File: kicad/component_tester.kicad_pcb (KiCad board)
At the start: 4 copper layers, 100.4 x 83 mm, 81 parts, among them IC201 MCP1640, IC202 ATmega328P-MMH, IC301 FT232RL, IC302 MAX1811, J301 0R-JUMPA, J302 0R-JUMPA, Q201 8 MHz, Q401 BSS138, Q402 BSS138, SW201 EVQ, T201 PMV65XP, T202 BSS84, T203 BSS123, T204 BC847, T301 BSS123, X201 MICRO-USB, X202 ISP

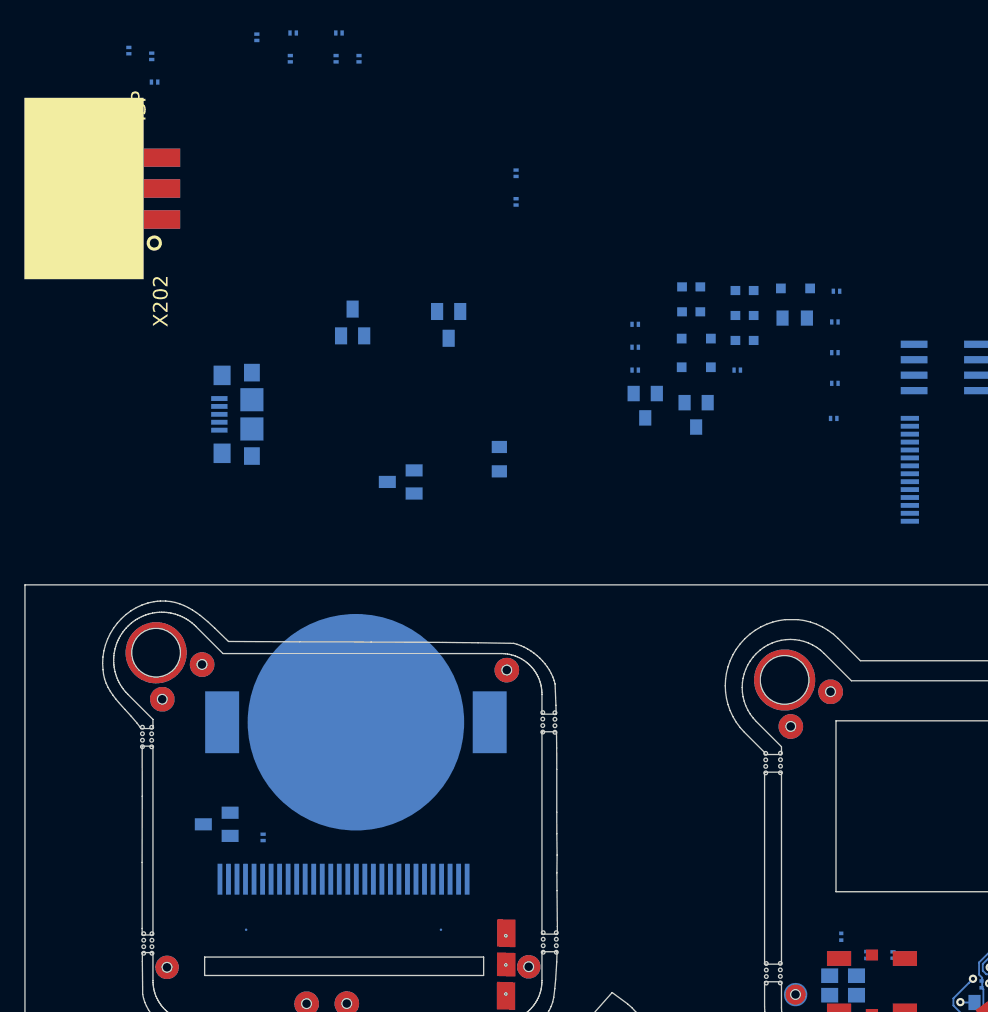
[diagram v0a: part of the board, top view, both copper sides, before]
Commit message: Make ISP header a pogo pin one
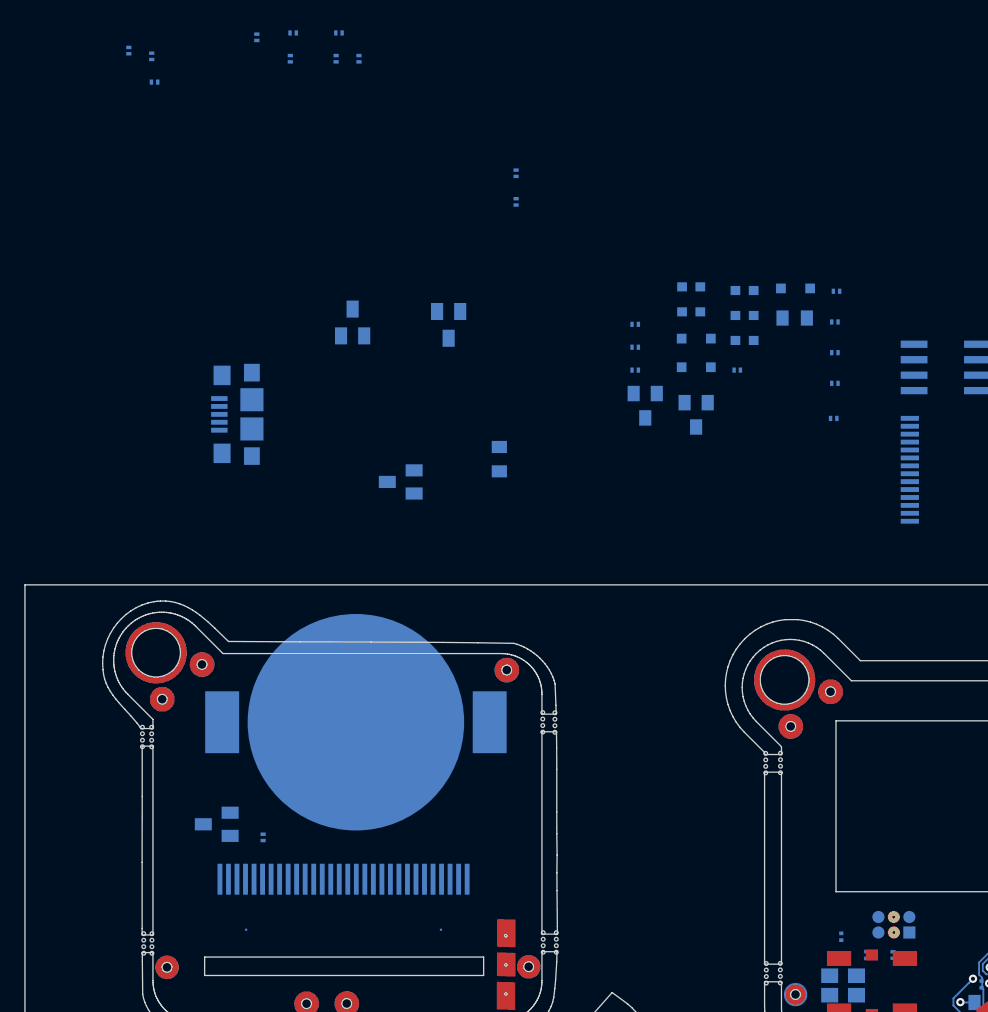
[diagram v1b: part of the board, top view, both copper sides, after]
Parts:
- X202: footprint component_tester:WANNE6_PCBKANTE -> component_tester:Pin_Header_Straight_2x03_Pitch1.27mm; moved to B.Cu
- moved X202 87.7 mm to (162.3, 105.2), turned to 90 degrees
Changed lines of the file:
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@@
     (mod_text_size 1 1)
     (mod_text_width 0.15)
-    (pad_size 0.8 0.8)
-    (pad_drill 0)
+    (pad_size 1 1)
+    (pad_drill 0.2)
     (pad_to_mask_clearance 0.2)
     (aux_axis_origin 0 0)
@@
       (outputformat 1)
       (mirror false)
-      (drillshape 1)
+      (drillshape 0)
       (scaleselection 1)
-      (outputdirectory ""))
+      (outputdirectory ../gerbers/))
   )
   (net 0 "")
@@
     (add_net VCC)
   )
+  (module component_tester:Pin_Header_Straight_2x03_Pitch1.27mm (layer Bottom)
+    (at 162.29 105.15 90)
+    (descr "Through hole straight pin header, 2x03, 1.27mm pitch, double rows")
+    (tags "Through hole pin header THT 2x03 1.27mm double row")
+    (fp_text reference X202 (at 0.635 1.695 90) (layer B.SilkS)
+      (effects (font (size 1 1) (thickness 0.15)) (justify mirror))
+    )
+    (fp_text value ISP (at 0.635 -4.235 90) (layer B.Fab)
+      (effects (font (size 1 1) (thickness 0.15)) (justify mirror))
+    )
+    (fp_line (start -0.2175 0.635) (end 2.34 0.635) (layer B.Fab) (width 0.1))
+    (fp_line (start 2.34 0.635) (end 2.34 -3.175) (layer B.Fab) (width 0.1))
+    (fp_line (start 2.34 -3.175) (end -1.07 -3.175) (layer B.Fab) (width 0.1))
+    (fp_line (start -1.07 -3.175) (end -1.07 -0.2175) (layer B.Fab) (width 0.1))
+    (fp_line (start -1.07 -0.2175) (end -0.2175 0.635) (layer B.Fab) (width 0.1))
+    (fp_line (start -1.13 -3.235) (end -0.30753 -3.235) (layer B.SilkS) (width 0.12))
+    (fp_line (start 1.57753 -3.235) (end 2.4 -3.235) (layer B.SilkS) (width 0.12))
+    (fp_line (start 0.30753 -3.235) (end 0.96247 -3.235) (layer B.SilkS) (width 0.12))
+    (fp_line (start -1.13 -0.76) (end -1.13 -3.235) (layer B.SilkS) (width 0.12))
+    (fp_line (start 2.4 0.695) (end 2.4 -3.235) (layer B.SilkS) (width 0.12))
+    (fp_line (start -1.13 -0.76) (end -0.563471 -0.76) (layer B.SilkS) (width 0.12))
+    (fp_line (start 0.563471 -0.76) (end 0.706529 -0.76) (layer B.SilkS) (width 0.12))
+    (fp_line (start 0.76 -0.706529) (end 0.76 -0.563471) (layer B.SilkS) (width 0.12))
+    (fp_line (start 0.76 0.563471) (end 0.76 0.695) (layer B.SilkS) (width 0.12))
+    (fp_line (start 0.76 0.695) (end 0.96247 0.695) (layer B.SilkS) (width 0.12))
+    (fp_line (start 1.57753 0.695) (end 2.4 0.695) (layer B.SilkS) (width 0.12))
+    (fp_line (start -1.13 0) (end -1.13 0.76) (layer B.SilkS) (width 0.12))
+    (fp_line (start -1.13 0.76) (end 0 0.76) (layer B.SilkS) (width 0.12))
+    (fp_line (start -1.6 1.15) (end -1.6 -3.7) (layer B.CrtYd) (width 0.05))
+    (fp_line (start -1.6 -3.7) (end 2.85 -3.7) (layer B.CrtYd) (width 0.05))
+    (fp_line (start 2.85 -3.7) (end 2.85 1.15) (layer B.CrtYd) (width 0.05))
+    (fp_line (start 2.85 1.15) (end -1.6 1.15) (layer B.CrtYd) (width 0.05))
+    (fp_text user %R (at 0.635 -1.27) (layer B.Fab)
+      (effects (font (size 1 1) (thickness 0.15)) (justify mirror))
+    )
+    (pad 1 smd rect (at 0 0 90) (size 1 1) (layers Bottom B.Paste B.Mask)
+      (net 15 "Net-(IC202-Pad14)"))
+    (pad 2 smd oval (at 1.27 0 90) (size 1 1) (layers Bottom B.Paste B.Mask)
+      (net 8 +5V))
+    (pad 3 thru_hole oval (at 0 -1.27 90) (size 1 1) (drill 0.2) (layers Bottom B.Mask)
+      (net 16 "Net-(IC202-Pad15)"))
+    (pad 4 thru_hole oval (at 1.27 -1.27 90) (size 1 1) (drill 0.2) (layers Bottom B.Mask)
+      (net 14 "Net-(IC202-Pad13)"))
+    (pad 5 smd oval (at 0 -2.54 90) (size 1 1) (layers Bottom B.Paste B.Mask)
+      (net 7 /component_tester_1/~RESET))
+    (pad 6 smd oval (at 1.27 -2.54 90) (size 1 1) (layers Bottom B.Paste B.Mask)
+      (net 1 GND))
+    (pad 3 thru_hole oval (at 0 -1.27 90) (size 0.4 0.4) (drill 0.2) (layers Top B.Mask)
+      (net 16 "Net-(IC202-Pad15)"))
+    (pad 4 thru_hole oval (at 1.27 -1.27 90) (size 0.4 0.4) (drill 0.2) (layers Top B.Mask)
+      (net 14 "Net-(IC202-Pad13)"))
+  )
   (module drawings:pads (layer Top)
     (at 170.763732 103.707786)
@@
       (solder_mask_margin 0.0762))
   )
-  (module component_tester:WANNE6_PCBKANTE (layer Top)
-    (at 99.41178 44.053294 180)
-    (fp_text reference X202 (at -0.7 -7.1 90) (layer F.SilkS)
-      (effects (font (size 1.2065 1.2065) (thickness 0.09652)) (justify right top))
-    )
-    (fp_text value ISP (at -0.3 5.5 90) (layer F.SilkS)
-      (effects (font (size 1.2065 1.2065) (thickness 0.09652)) (justify left bottom))
-    )
-    (fp_poly (pts (xy 0.1 1.6) (xy 2.1 1.6) (xy 2.1 -1.5) (xy 0.1 -1.5)) (layer F.Fab) (width 0))
-    (fp_poly (pts (xy 0 7.45) (xy 9.8 7.45) (xy 9.8 -7.45) (xy 0 -7.45)) (layer B.SilkS) (width 0))
-    (fp_poly (pts (xy 0 7.45) (xy 9.8 7.45) (xy 9.8 -7.45) (xy 0 -7.45)) (layer F.SilkS) (width 0))
-    (fp_circle (center -0.87 -4.48) (end -0.37 -4.48) (layer F.SilkS) (width 0.254))
-    (pad P$6 smd rect (at -1.5 2.54 180) (size 3 1.5) (layers Bottom B.Paste B.Mask)
-      (net 1 GND) (solder_mask_margin 0.0762))
-    (pad P$4 smd rect (at -1.5 0 180) (size 3 1.5) (layers Bottom B.Paste B.Mask)
-      (net 14 "Net-(IC202-Pad13)") (solder_mask_margin 0.0762))
-    (pad P$2 smd rect (at -1.5 -2.54 180) (size 3 1.5) (layers Bottom B.Paste B.Mask)
-      (net 8 +5V) (solder_mask_margin 0.0762))
-    (pad P$5 smd rect (at -1.5 2.54) (size 3 1.5) (layers Top F.Paste F.Mask)
-      (net 7 /component_tester_1/~RESET) (solder_mask_margin 0.0762))
-    (pad P$1 smd rect (at -1.5 -2.54) (size 3 1.5) (layers Top F.Paste F.Mask)
-      (net 15 "Net-(IC202-Pad14)") (solder_mask_margin 0.0762))
-    (pad P$3 smd rect (at -1.5 0) (size 3 1.5) (layers Top F.Paste F.Mask)
-      (net 16 "Net-(IC202-Pad15)") (solder_mask_margin 0.0762))
-  )
   (module component_tester:SOT23 (layer Bottom)

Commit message: Work on placing/routing
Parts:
- C202: footprint KiCad/Capacitors_SMD.pretty:C_0201 -> KiCad/Capacitors_SMD.pretty:C_0402
- moved R212 115.1 mm to (204.3, 82.0)
- moved R203 115.1 mm to (219.7, 80.1)
- moved R205 115.1 mm to (215.9, 80.1)
- moved R202 115.1 mm to (221.4, 82.2)
- moved R204 115.1 mm to (213.0, 80.4)
- moved R208 115.1 mm to (219.5, 82.2)
- moved R210 115.1 mm to (215.7, 82.2)
- moved R211 115.1 mm to (202.5, 81.5)
- moved R213 115.1 mm to (204.6, 84.1)
- moved D201 107.4 mm to (218.8, 87.8)
- moved R209 97.4 mm to (218.3, 83.9)
- moved R207 96.4 mm to (215.4, 89.7)
- moved D202 94.2 mm to (212.8, 86.9)
- moved T203 88.8 mm to (206.8, 88.4)
- moved X202 6.52 mm to (168.8, 105.1)
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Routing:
- net Net-(C209-Pad1): track 4.05 -> 21.0 mm, vias 0 -> 2
- net Net-(C210-Pad1): track 18.7 -> 27.4 mm
- net +5V: track 11.3 -> 3.01 mm, vias 2 -> 0
- net Net-(IC202-Pad14): track 16.6 -> 9.91 mm
- net Net-(C208-Pad1): track 29.2 -> 35.7 mm
- net Net-(IC202-Pad15): track 18.9 -> 22.9 mm
- net GND: track 16.8 -> 15.3 mm
- net Net-(C206-Pad2): track 2.13 -> 3.25 mm
- added copper zone on In2.Cu, net GND
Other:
- net class Thin added: clearance 0.1, trace_width 0.1, via_dia 0.35, via_drill 0.2
- rule trace_min: 0.1524 -> 0.1
- rule via_min_drill: 0.254 -> 0.2
- rule via_min_size: 0.508 -> 0.35

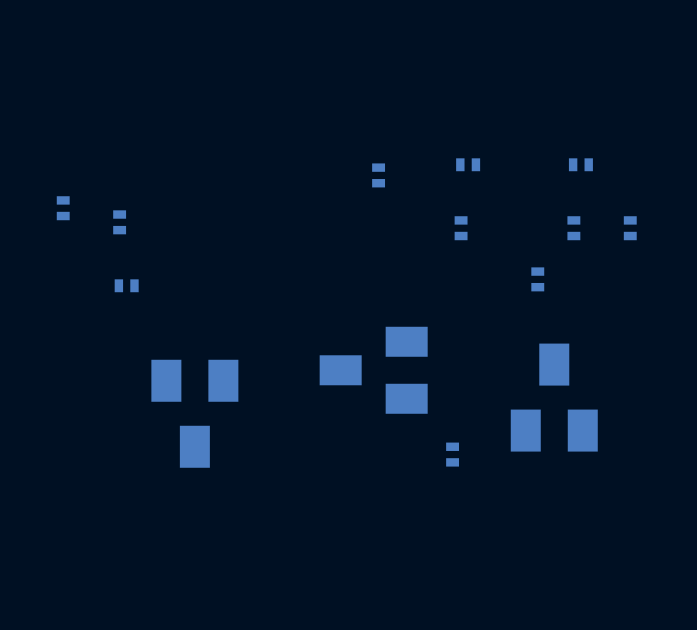
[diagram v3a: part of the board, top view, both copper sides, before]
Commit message: Cut out precision voltage reference
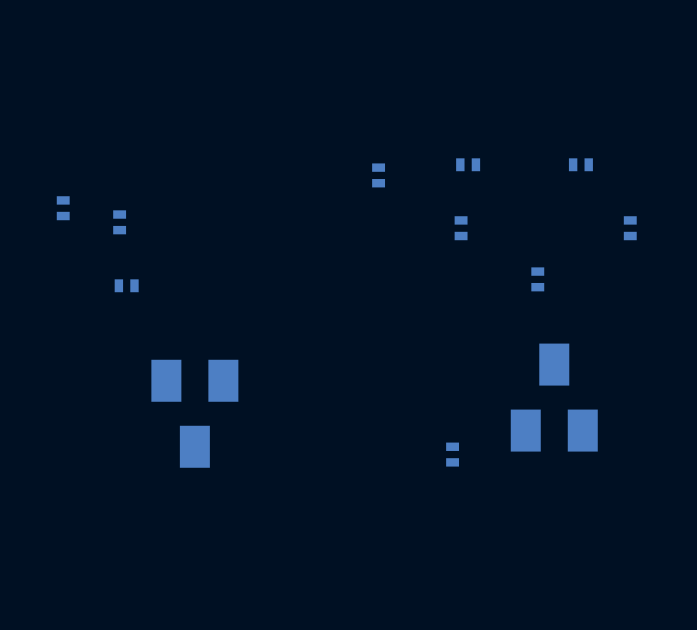
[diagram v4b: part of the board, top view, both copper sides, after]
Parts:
- removed D202: LM4040A-2V5, component_tester:SOT23
- removed R208: 47k, KiCad/Resistors_SMD.pretty:R_0201

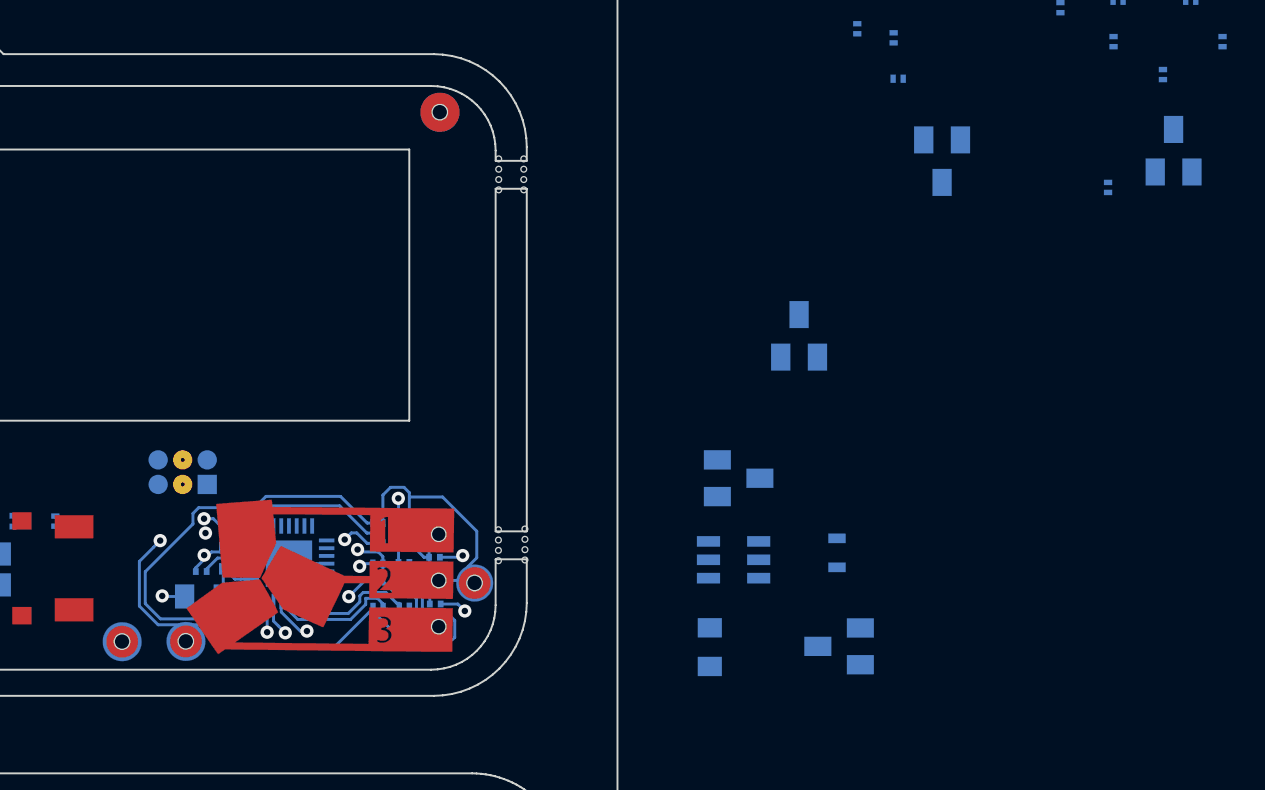
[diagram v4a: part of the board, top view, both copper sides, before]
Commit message: Switch some transistors for smaller footprints
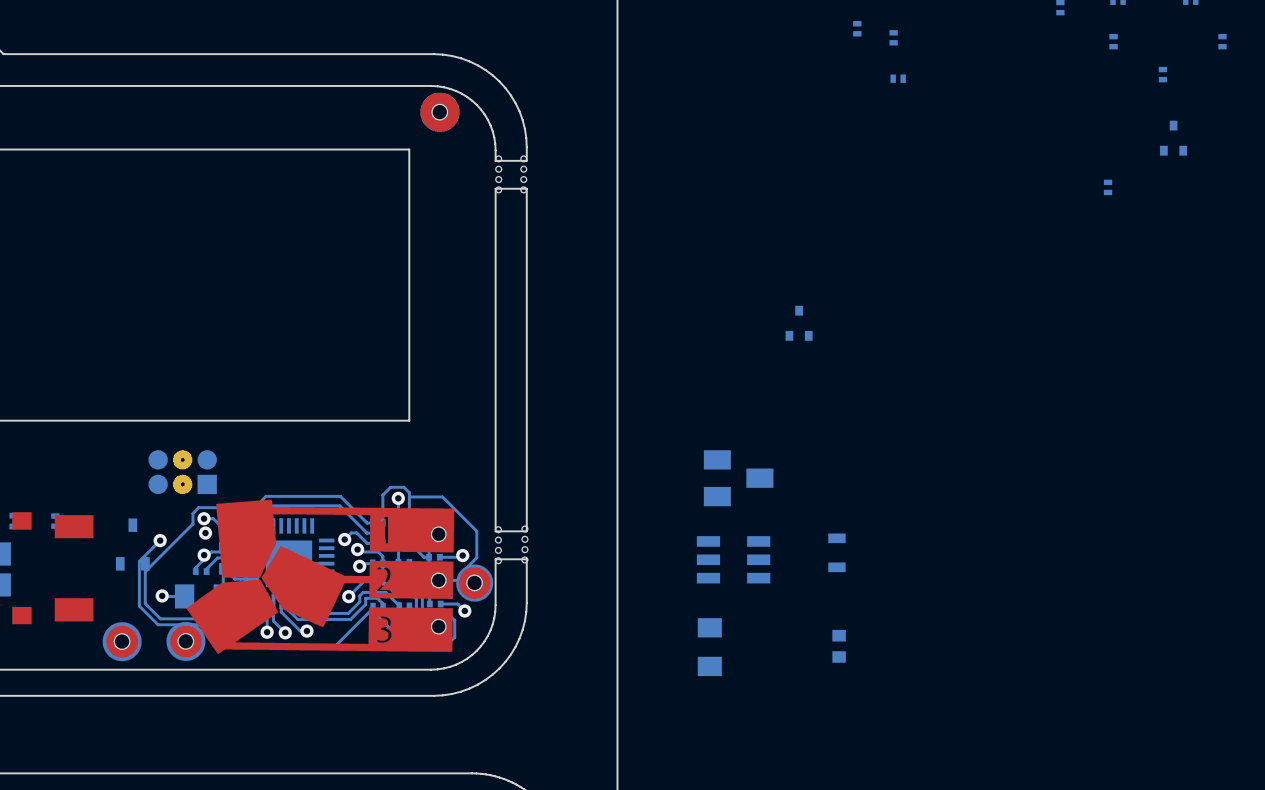
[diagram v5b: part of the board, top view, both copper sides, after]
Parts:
- D201, T204: footprint component_tester:SOT23 -> digikey/digikey-kicad-library/src/Source_Footprints:SOT-523
- D203: footprint component_tester:SOT23 -> KiCad/LEDs.pretty:LED_0402
- T203: footprint component_tester:SOT23 -> KiCad/TO_SOT_Packages_SMD.pretty:SOT-323_SC-70
- moved T203 46.3 mm to (165.0, 108.2), turned to 90 degrees

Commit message: Route some more
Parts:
- moved C202 0.08 mm to (169.6, 108.9)
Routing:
- net Net-(IC202-Pad9): track 0.00 -> 17.6 mm, vias 0 -> 2
- net Net-(C208-Pad1): track 35.7 -> 39.6 mm
- net GND: track 15.3 -> 13.5 mm, vias 5 -> 4
- net Net-(IC202-Pad11): track 6.31 -> 7.96 mm
- net Net-(IC202-Pad10): track 6.71 -> 8.34 mm

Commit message: Place and route
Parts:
- moved T203 1.71 mm to (164.4, 109.8)
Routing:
- net Net-(D203-Pad1): track 0.00 -> 9.97 mm, vias 0 -> 1
- net GND: track 13.5 -> 19.5 mm, vias 4 -> 6
- net Net-(IC202-Pad15): track 22.7 -> 22.0 mm
- net Net-(C208-Pad1): track 39.6 -> 39.0 mm

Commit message: Route stuff
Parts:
- moved R204 55.7 mm to (164.3, 107.4), turned to 180 degrees
- moved T301 8.40 mm to (179.0, 63.5)
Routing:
- net /component_tester_1/~RESET: track 0.00 -> 9.52 mm, vias 0 -> 1
- net Net-(C210-Pad1): track 27.4 -> 28.6 mm
- net Net-(IC202-Pad15): track 22.0 -> 22.9 mm
